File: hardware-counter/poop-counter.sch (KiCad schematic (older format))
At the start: 6 parts, among them J0 USB_C_Receptacle, U0 ESP8266EX

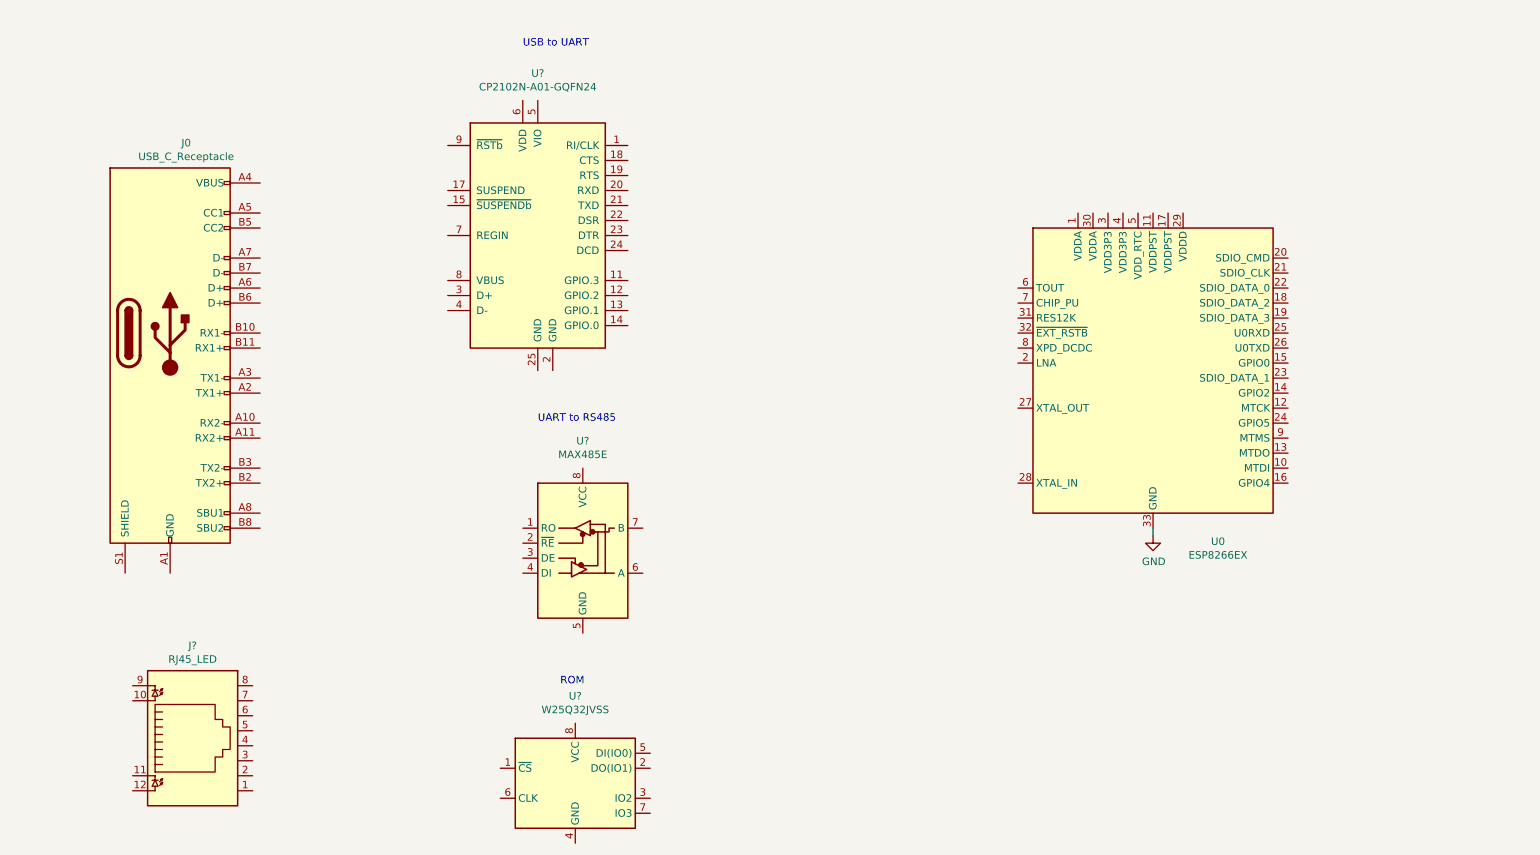
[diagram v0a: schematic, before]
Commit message: voltage regulation and decoupling for mcu
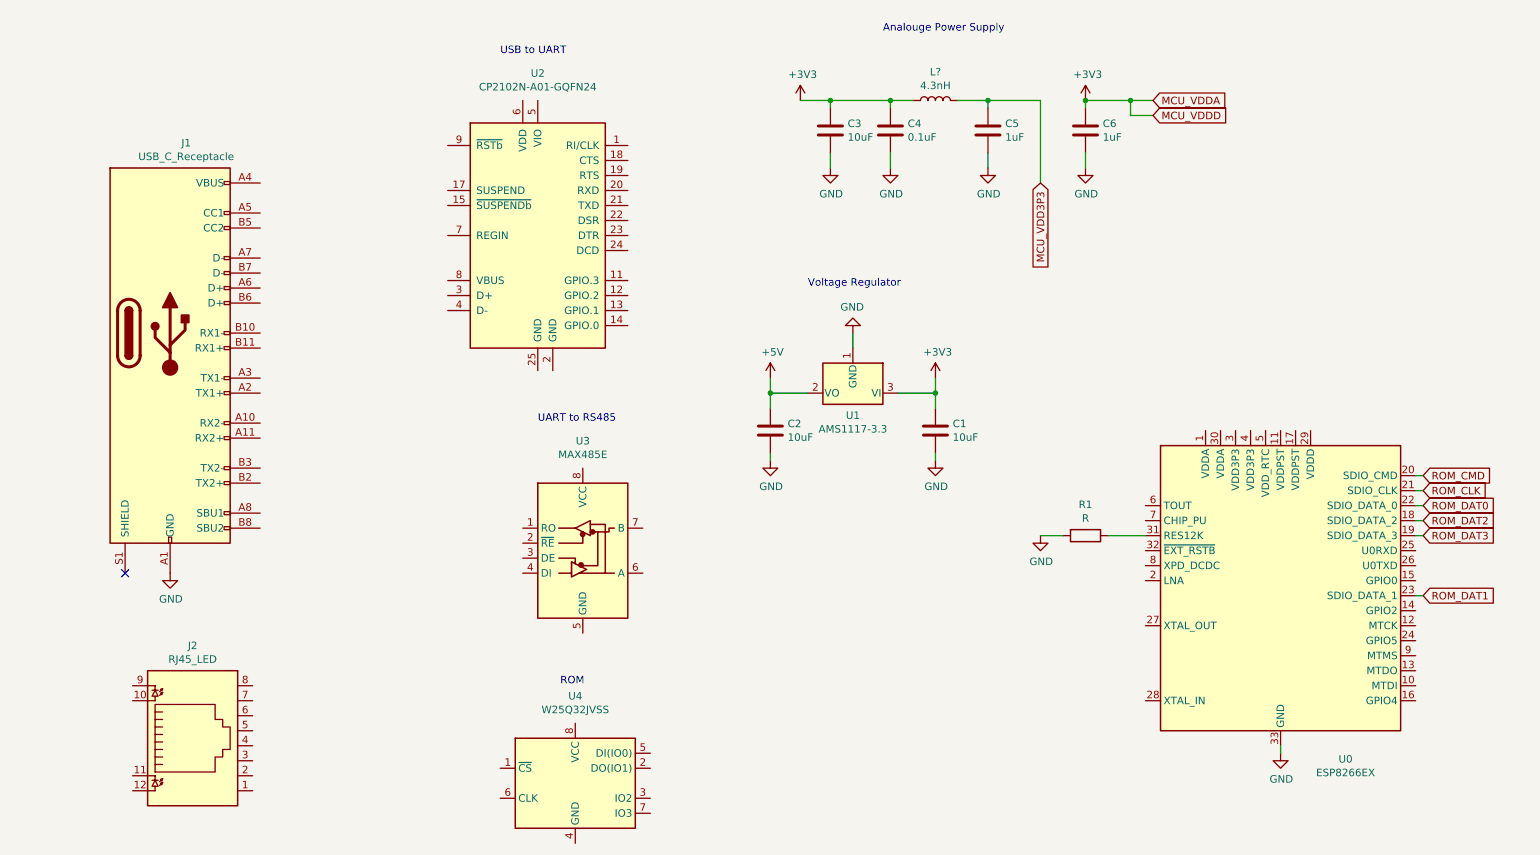
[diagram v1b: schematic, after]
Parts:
- added C1, C2, C3: 10uF, symbol Device:C
- added C4: 0.1uF, symbol Device:C
- added C5, C6: 1uF, symbol Device:C
- added L?: 4.3nH, symbol Device:L
- added R1: R, symbol Device:R
- added U1: AMS1117-3.3, Package_TO_SOT_SMD:SOT-223-3_TabPin2, symbol Regulator_Linear:AMS1117-3.3
- gave numbers to parts that had none: 4
- renumbered J0 to J1
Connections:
- net GND: now also J1.A1 (GND), J1.A12 (GND), J1.B1 (GND), J1.B12 (GND), C1.2, C2.1, C3.2, C4.2, C5.2, C6.2, R1.2, U1.1 (GND)
- net ROM_DAT2: now reaches U0.18 (SDIO_DATA_2)
- net ROM_DAT3: now reaches U0.19 (SDIO_DATA_3)
- net ROM_CMD: now reaches U0.20 (SDIO_CMD)
- net ROM_CLK: now reaches U0.21 (SDIO_CLK)
- net ROM_DAT0: now reaches U0.22 (SDIO_DATA_0)
- net ROM_DAT1: now reaches U0.23 (SDIO_DATA_1)
- net at U0.31 (RES12K): now also R1.1
- new net +3V3: C1.1, C3.1, C4.1, C6.1, L?.1, U1.3 (VI)
- new net +5V: C2.2, U1.2 (VO)
- new net MCU_VDD3P3: C5.1, L?.2
- no-connect marks 0 -> 1
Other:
- note added: "Analouge Power Supply"
- note added: "Voltage Regulator"
- moved on the sheet: U0

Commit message: changes ennit
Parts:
- added AE1: Antenna_Loop, symbol Device:Antenna_Loop
- added C10: 3pF, symbol Device:C
- added C7, C8: 10pF, symbol Device:C
- added C9: 2.4pF, symbol Device:C
- added L2: 2.2nH, symbol Device:L
- added R?: 499, symbol Device:R
- added Y1: 24Mhz±10ppm, symbol Device:Crystal_GND24
- R1: value R -> 12k
- gave numbers to parts that had none: 1
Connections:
- net +3V3: now also U0.1 (VDDA), U0.11 (VDDPST), U0.17 (VDDPST), U0.29 (VDDD), U0.30 (VDDA)
- net GND: now also AE1.1, C10.2, C7.2, C8.2, C9.2, Y1.2, Y1.4
- net MCU_VDD3P3: now also U0.3 (VDD3P3), U0.4 (VDD3P3)
- net ROM_CLK: now also U0.12 (MTCK); no longer U0.21 (SDIO_CLK)
- net ANTENNA: now reaches U0.2 (LNA)
- net ANTENNA: now also C10.1, L2.2
- net OSC_OUT: now reaches U0.27 (XTAL_OUT)
- net OSC_OUT: now also C8.1, Y1.3
- net OSC_IN: now reaches U0.28 (XTAL_IN)
- net OSC_IN: now also C7.1, Y1.1
- new net: AE1.2, C9.1, L2.1
- no-connect marks 1 -> 2
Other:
- note added: "Crystal Oscillator"
- note added: "WiFi Antenna"
- moved on the sheet: C1, C2, J1, J2, U1, U2, U3, U4
